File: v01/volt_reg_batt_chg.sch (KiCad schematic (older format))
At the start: 13 parts

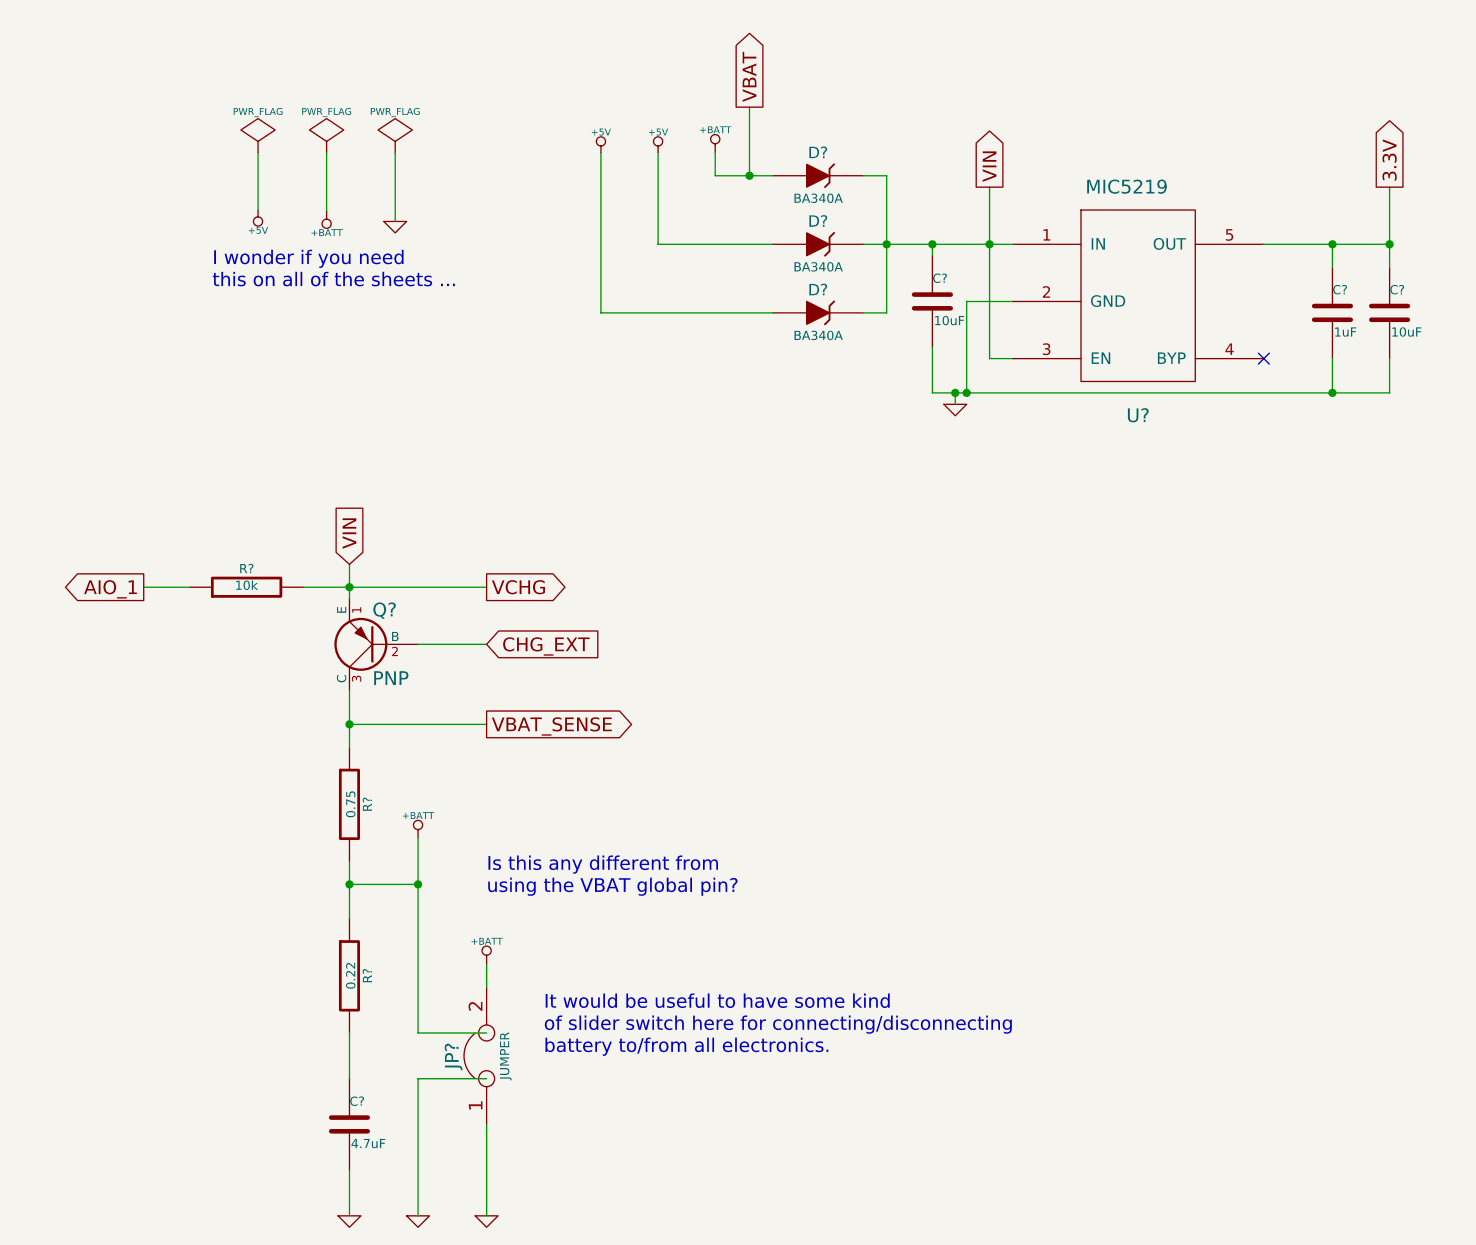
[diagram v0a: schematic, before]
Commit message: Basically just added a single DIP switch to battery charging circuit.
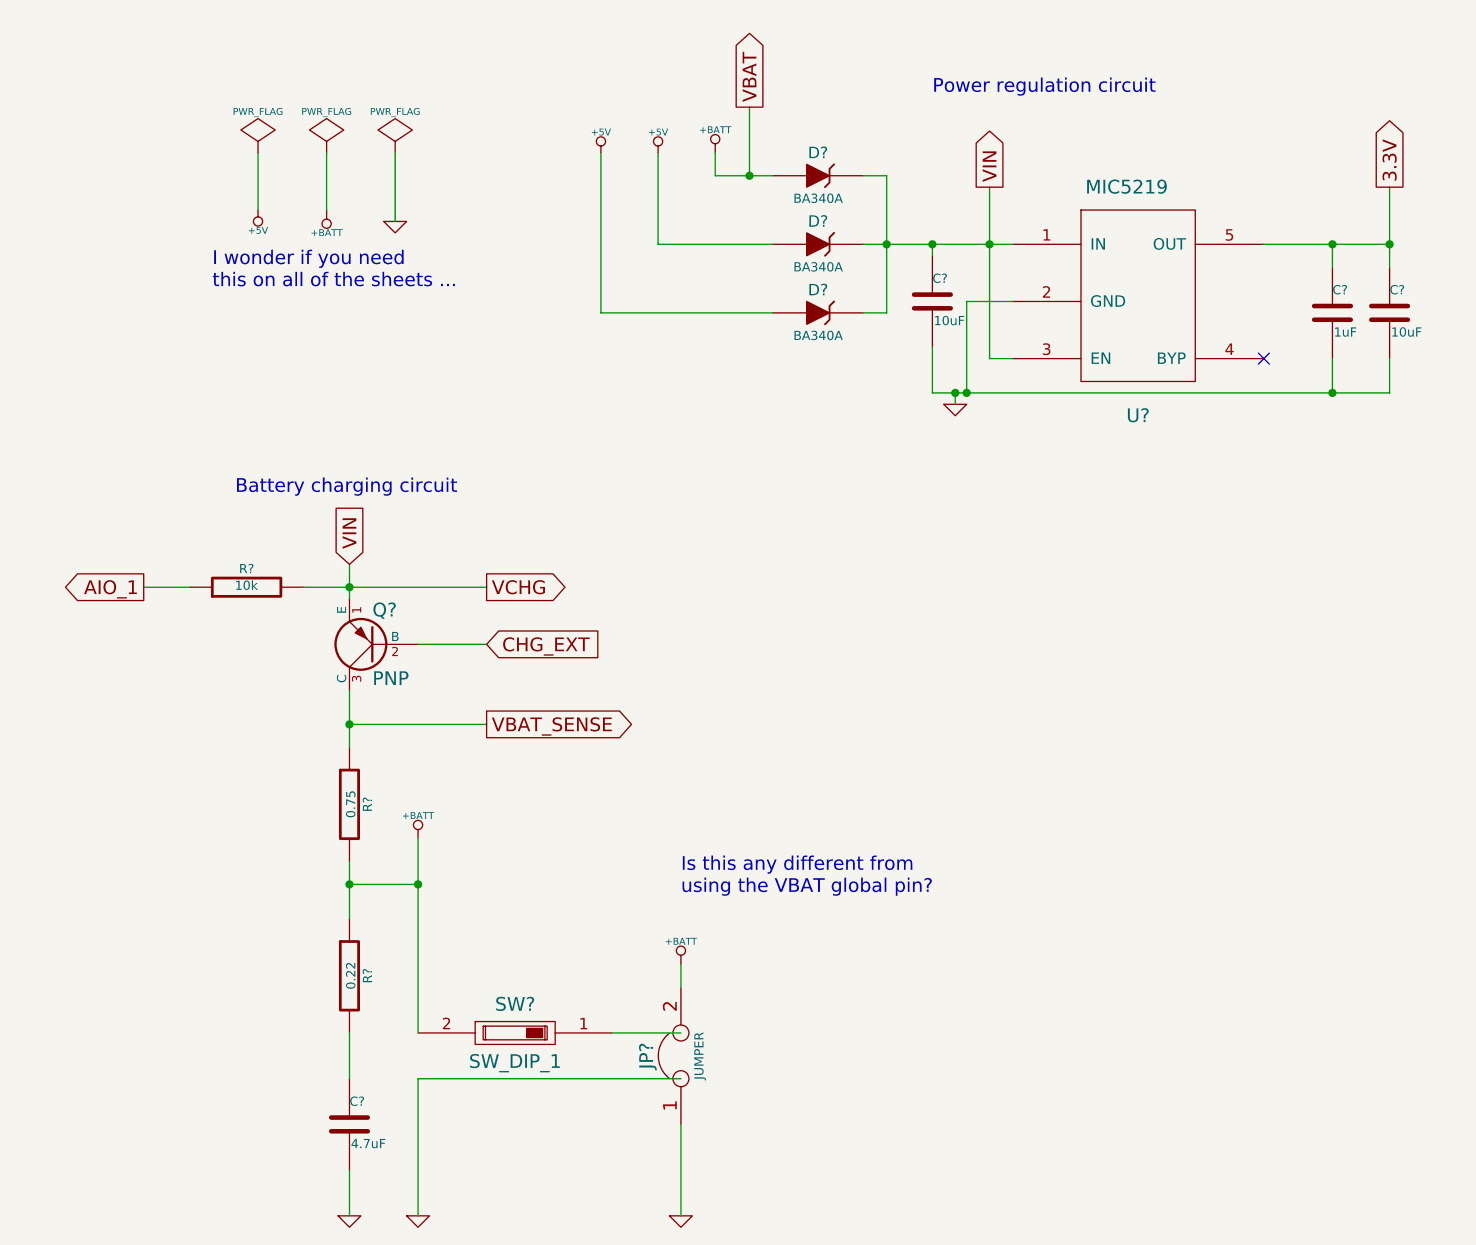
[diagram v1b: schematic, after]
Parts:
- added SW?: SW_DIP_1, symbol SW_DIP_1
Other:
- note added: "Battery charging circuit"
- note added: "Power regulation circuit"
- note removed: "It would be useful to have some kind \nof slider switch here for connecting/disconnecting \nbattery to/from all electronics."
- moved on the sheet: JP?
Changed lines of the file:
@@
 Sheet 4 4
 Title ""
-Date "12 oct 2014"
+Date "18 oct 2014"
 Rev ""
 Comp ""
@@
 L JUMPER JP?
 U 1 1 5439CFCC
-P 2850 5550
-F 0 "JP?" H 2850 5700 60  0000 C CNN
-F 1 "JUMPER" H 2850 5470 40  0000 C CNN
-F 2 "~" H 2850 5550 60  0000 C CNN
-F 3 "~" H 2850 5550 60  0000 C CNN
-	1    2850 5550
+P 3700 5550
+F 0 "JP?" H 3700 5700 60  0000 C CNN
+F 1 "JUMPER" H 3700 5470 40  0000 C CNN
+F 2 "~" H 3700 5550 60  0000 C CNN
+F 3 "~" H 3700 5550 60  0000 C CNN
+	1    3700 5550
 	0    -1   -1   0
 $EndComp
@@
 L GND #PWR?
 U 1 1 5439D2F7
-P 2850 6250
-F 0 "#PWR?" H 2850 6250 30  0001 C CNN
-F 1 "GND" H 2850 6180 30  0001 C CNN
-F 2 "" H 2850 6250 60  0000 C CNN
-F 3 "" H 2850 6250 60  0000 C CNN
-	1    2850 6250
+P 3700 6250
+F 0 "#PWR?" H 3700 6250 30  0001 C CNN
+F 1 "GND" H 3700 6180 30  0001 C CNN
+F 2 "" H 3700 6250 60  0000 C CNN
+F 3 "" H 3700 6250 60  0000 C CNN
+	1    3700 6250
 	1    0    0    -1
 $EndComp
@@
 L +BATT #PWR?
 U 1 1 5439D33F
-P 2850 5150
-F 0 "#PWR?" H 2850 5100 20  0001 C CNN
-F 1 "+BATT" H 2850 5250 30  0000 C CNN
-F 2 "" H 2850 5150 60  0000 C CNN
-F 3 "" H 2850 5150 60  0000 C CNN
-	1    2850 5150
+P 3700 5150
+F 0 "#PWR?" H 3700 5100 20  0001 C CNN
+F 1 "+BATT" H 3700 5250 30  0000 C CNN
+F 2 "" H 3700 5150 60  0000 C CNN
+F 3 "" H 3700 5150 60  0000 C CNN
+	1    3700 5150
 	1    0    0    -1
 $EndComp
@@
 Text GLabel 1350 3500 0    60   Output ~ 0
 AIO_1
+Text Notes 1650 2200 0    60   ~ 0
+I wonder if you need\nthis on all of the sheets ...
+Text Notes 3700 4850 0    60   ~ 0
+Is this any different from \nusing the VBAT global pin?
 Wire Wire Line
 	4500 2000 5150 2000
@@
 	2250 3950 2250 4200
 Wire Wire Line
-	4100 1700 3850 1700
+	3850 1700 4100 1700
 Wire Wire Line
 	3850 1700 3850 1600
@@
 	2250 3400 2250 3550
 Wire Wire Line
-	2550 5450 2850 5450
+	3400 5450 3700 5450
 Wire Wire Line
 	2550 4600 2550 5450
@@
 Connection ~ 2250 4800
 Wire Wire Line
-	2550 5650 2850 5650
-Wire Wire Line
 	2550 5650 2550 6250
 Connection ~ 2550 4800
@@
 Connection ~ 2250 3500
 Wire Wire Line
-	2850 5850 2850 6250
-Wire Wire Line
-	2850 5150 2850 5250
+	3700 5850 3700 6250
+Wire Wire Line
+	3700 5150 3700 5250
 Wire Wire Line
 	4000 1400 4000 1700
@@
 Wire Wire Line
 	1550 3500 1350 3500
-Text Notes 3100 5550 0    60   ~ 0
-It would be useful to have some kind \nof slider switch here for connecting/disconnecting \nbattery to/from all electronics.
-Text Notes 1650 2200 0    60   ~ 0
-I wonder if you need\nthis on all of the sheets ...
-Text Notes 2850 4850 0    60   ~ 0
-Is this any different from \nusing the VBAT global pin?
+$Comp
+L SW_DIP_1 SW?
+U 1 1 5442B59A
+P 2975 5450
+F 0 "SW?" H 2975 5575 60  0000 C CNN
+F 1 "SW_DIP_1" H 2975 5325 60  0000 C CNN
+F 2 "" H 2975 5450 60  0000 C CNN
+F 3 "" H 2975 5450 60  0000 C CNN
+	1    2975 5450
+	1    0    0    -1
+$EndComp
+Text Notes 1750 3100 0    60   ~ 0
+Battery charging circuit
+Text Notes 4800 1350 0    60   ~ 0
+Power regulation circuit
+Wire Wire Line
+	2550 5650 3700 5650
 $EndSCHEMATC

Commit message: ERC.
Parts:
- removed D?: BA340A, ~, symbol ZENER
- removed SW?: SW_DIP_1, symbol SW_DIP_1
- gave numbers to parts that had none: 12
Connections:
- net labels added: 5V_USB
- wire segments 43 -> 40
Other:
- note added: "I wonder if you need\nthis on all of the sheets ... No."
- note added: "It would be useful to have some kind \nof slider switch here for connecting/disconnecting \nbattery to/from all electronics."
- note added: "So, the voltages (+5V, GND, +BATT) are considered power inputs,\n while the power flags are considered power outputs. So, throughout\nthe schematic, components need to specify power pins as power input\n pins because they are being driven by the power flag (power output) \nnot the voltages (power input).\n"
- note removed: "Battery charging circuit"
- note removed: "I wonder if you need\nthis on all of the sheets ..."
- note removed: "Power regulation circuit"
- moved on the sheet: JP1

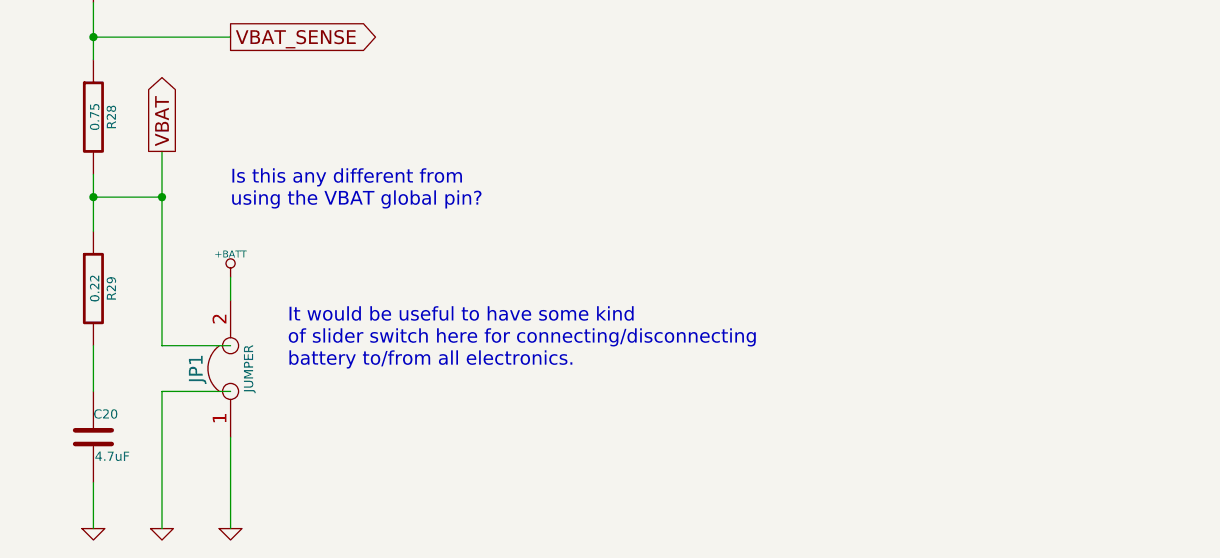
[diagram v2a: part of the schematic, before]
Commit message: updates:
1) added DIP-1 switch to connect/disconnect battery
2) annotated components in the entire schematic
3) generated netlist for the schematic
4) matched components with footprints (caps, DIP switch, diodes, LEDs, I think that's it ...)
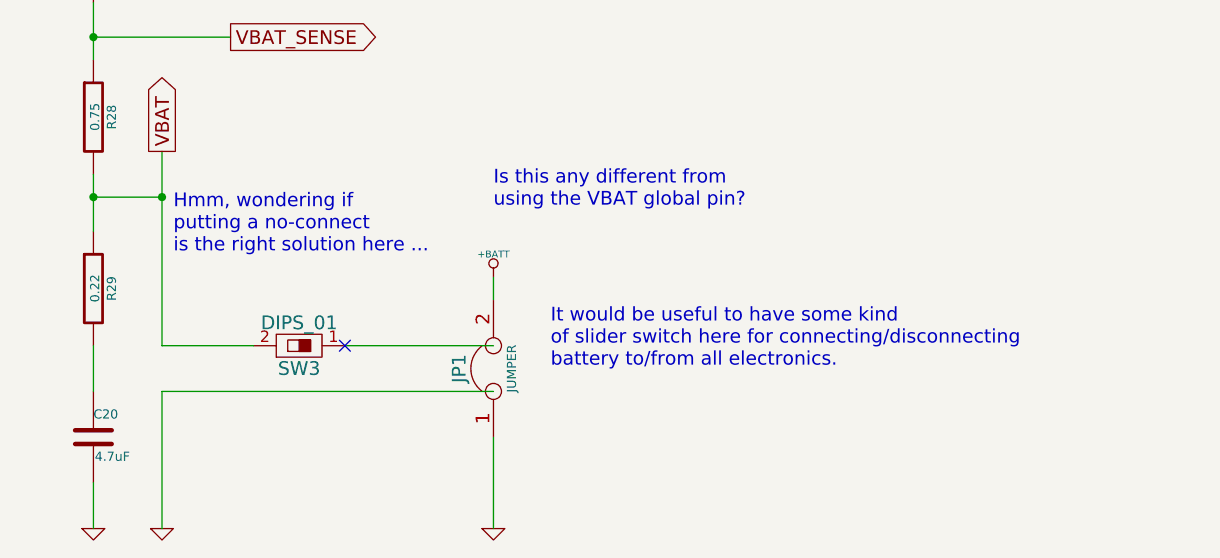
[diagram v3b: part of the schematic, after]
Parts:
- added SW3: DIPS_01, symbol DIPS_01
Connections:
- wire segments 40 -> 41
- no-connect marks 1 -> 2
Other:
- note added: "Hmm, wondering if \nputting a no-connect\nis the right solution here ..."
- moved on the sheet: JP1
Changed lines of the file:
@@
 LIBS:BC127
 LIBS:mic5219
+LIBS:ab2_usb
 LIBS:CWIEM_PCB_v01-cache
 EELAYER 27 0
@@
 L JUMPER JP1
 U 1 1 5439CFCC
-P 2850 5550
-F 0 "JP1" H 2850 5700 60  0000 C CNN
-F 1 "JUMPER" H 2850 5470 40  0000 C CNN
-F 2 "~" H 2850 5550 60  0000 C CNN
-F 3 "~" H 2850 5550 60  0000 C CNN
-	1    2850 5550
+P 4000 5550
+F 0 "JP1" H 4000 5700 60  0000 C CNN
+F 1 "JUMPER" H 4000 5470 40  0000 C CNN
+F 2 "~" H 4000 5550 60  0000 C CNN
+F 3 "~" H 4000 5550 60  0000 C CNN
+	1    4000 5550
 	0    -1   -1   0
 $EndComp
@@
 L GND #PWR018
 U 1 1 5439D2F7
-P 2850 6250
-F 0 "#PWR018" H 2850 6250 30  0001 C CNN
-F 1 "GND" H 2850 6180 30  0001 C CNN
-F 2 "" H 2850 6250 60  0000 C CNN
-F 3 "" H 2850 6250 60  0000 C CNN
-	1    2850 6250
+P 4000 6250
+F 0 "#PWR018" H 4000 6250 30  0001 C CNN
+F 1 "GND" H 4000 6180 30  0001 C CNN
+F 2 "" H 4000 6250 60  0000 C CNN
+F 3 "" H 4000 6250 60  0000 C CNN
+	1    4000 6250
 	1    0    0    -1
 $EndComp
@@
 L +BATT #PWR019
 U 1 1 5439D33F
-P 2850 5150
-F 0 "#PWR019" H 2850 5100 20  0001 C CNN
-F 1 "+BATT" H 2850 5250 30  0000 C CNN
-F 2 "" H 2850 5150 60  0000 C CNN
-F 3 "" H 2850 5150 60  0000 C CNN
-	1    2850 5150
+P 4000 5150
+F 0 "#PWR019" H 4000 5100 20  0001 C CNN
+F 1 "+BATT" H 4000 5250 30  0000 C CNN
+F 2 "" H 4000 5150 60  0000 C CNN
+F 3 "" H 4000 5150 60  0000 C CNN
+	1    4000 5150
 	1    0    0    -1
 $EndComp
@@
 	2250 3400 2250 3550
 Wire Wire Line
-	2550 5450 2850 5450
+	3350 5450 4000 5450
 Wire Wire Line
 	2550 4600 2550 5450
@@
 Connection ~ 2250 4800
 Wire Wire Line
-	2550 5650 2850 5650
+	2550 5650 4000 5650
 Wire Wire Line
 	2550 5650 2550 6250
@@
 Connection ~ 2250 3500
 Wire Wire Line
-	2850 5850 2850 6250
-Wire Wire Line
-	2850 5150 2850 5250
+	4000 5850 4000 6250
+Wire Wire Line
+	4000 5150 4000 5250
 Connection ~ 4000 1700
 Wire Wire Line
 	1550 3500 1350 3500
-Text Notes 3100 5550 0    60   ~ 0
+Text Notes 4250 5550 0    60   ~ 0
 It would be useful to have some kind \nof slider switch here for connecting/disconnecting \nbattery to/from all electronics.
 Text Notes 1300 2200 0    60   ~ 0
 I wonder if you need\nthis on all of the sheets ... No.
-Text Notes 2850 4850 0    60   ~ 0
+Text Notes 4000 4850 0    60   ~ 0
 Is this any different from \nusing the VBAT global pin?
 Wire Wire Line
@@
 Wire Wire Line
 	3550 2300 4100 2300
+Wire Wire Line
+	2550 5450 2950 5450
+$Comp
+L DIPS_01 SW3
+U 1 1 544BE30E
+P 3150 5450
+F 0 "SW3" V 3050 5450 60  0000 C CNN
+F 1 "DIPS_01" V 3250 5450 60  0000 C CNN
+F 2 "" H 3150 5450 60  0000 C CNN
+F 3 "" H 3150 5450 60  0000 C CNN
+	1    3150 5450
+	0    -1   -1   0
+$EndComp
+NoConn ~ 3350 5450
+Text Notes 2600 5050 0    60   ~ 0
+Hmm, wondering if \nputting a no-connect\nis the right solution here ...
 $EndSCHEMATC

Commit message: Updating with latest edits (haven't committed in a while)
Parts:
- removed JP1: JUMPER, ~, symbol JUMPER
- added P13: JST-PH2, jst-ph-JST-PH2, symbol JST-PH2
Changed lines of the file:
@@
 LIBS:mic5219
 LIBS:ab2_usb
+LIBS:jst-ph
 LIBS:CWIEM_PCB_v01-cache
 EELAYER 27 0
@@
 Sheet 4 4
 Title ""
-Date "25 oct 2014"
+Date "7 dec 2014"
 Rev ""
 Comp ""
@@
 $EndComp
 $Comp
-L GND #PWR013
+L GND #PWR18
 U 1 1 5439B1A3
 P 4900 2700
-F 0 "#PWR013" H 4900 2700 30  0001 C CNN
+F 0 "#PWR18" H 4900 2700 30  0001 C CNN
 F 1 "GND" H 4900 2630 30  0001 C CNN
 F 2 "" H 4900 2700 60  0000 C CNN
@@
 $EndComp
 $Comp
-L GND #PWR014
+L GND #PWR15
 U 1 1 5439B578
 P 2250 6250
-F 0 "#PWR014" H 2250 6250 30  0001 C CNN
+F 0 "#PWR15" H 2250 6250 30  0001 C CNN
 F 1 "GND" H 2250 6180 30  0001 C CNN
 F 2 "" H 2250 6250 60  0000 C CNN
@@
 3.3V
 $Comp
-L PWR_FLAG #FLG015
+L PWR_FLAG #FLG2
 U 1 1 5439CBDC
 P 2150 1600
-F 0 "#FLG015" H 2150 1695 30  0001 C CNN
+F 0 "#FLG2" H 2150 1695 30  0001 C CNN
 F 1 "PWR_FLAG" H 2150 1780 30  0000 C CNN
 F 2 "" H 2150 1600 60  0000 C CNN
@@
 $EndComp
 $Comp
-L +BATT #PWR016
+L +BATT #PWR14
 U 1 1 5439CC42
 P 2150 1850
-F 0 "#PWR016" H 2150 1800 20  0001 C CNN
+F 0 "#PWR14" H 2150 1800 20  0001 C CNN
 F 1 "+BATT" H 2150 1950 30  0000 C CNN
 F 2 "" H 2150 1850 60  0000 C CNN
@@
 VIN
 $Comp
-L JUMPER JP1
-U 1 1 5439CFCC
-P 4000 5550
-F 0 "JP1" H 4000 5700 60  0000 C CNN
-F 1 "JUMPER" H 4000 5470 40  0000 C CNN
-F 2 "~" H 4000 5550 60  0000 C CNN
-F 3 "~" H 4000 5550 60  0000 C CNN
-	1    4000 5550
-	0    -1   -1   0
-$EndComp
-$Comp
-L GND #PWR017
+L GND #PWR17
 U 1 1 5439D063
 P 2550 6250
-F 0 "#PWR017" H 2550 6250 30  0001 C CNN
+F 0 "#PWR17" H 2550 6250 30  0001 C CNN
 F 1 "GND" H 2550 6180 30  0001 C CNN
 F 2 "" H 2550 6250 60  0000 C CNN
@@
 Text GLabel 2850 3750 2    60   Input ~ 0
 CHG_EXT
-$Comp
-L GND #PWR018
-U 1 1 5439D2F7
-P 4000 6250
-F 0 "#PWR018" H 4000 6250 30  0001 C CNN
-F 1 "GND" H 4000 6180 30  0001 C CNN
-F 2 "" H 4000 6250 60  0000 C CNN
-F 3 "" H 4000 6250 60  0000 C CNN
-	1    4000 6250
-	1    0    0    -1
-$EndComp
-$Comp
-L +BATT #PWR019
-U 1 1 5439D33F
-P 4000 5150
-F 0 "#PWR019" H 4000 5100 20  0001 C CNN
-F 1 "+BATT" H 4000 5250 30  0000 C CNN
-F 2 "" H 4000 5150 60  0000 C CNN
-F 3 "" H 4000 5150 60  0000 C CNN
-	1    4000 5150
-	1    0    0    -1
-$EndComp
 $Comp
 L R R27
@@
 	2250 3400 2250 3550
 Wire Wire Line
-	3350 5450 4000 5450
+	3350 5450 3600 5450
 Wire Wire Line
 	2550 4600 2550 5450
@@
 Connection ~ 2250 4800
 Wire Wire Line
-	2550 5650 4000 5650
+	2550 5650 3600 5650
 Wire Wire Line
 	2550 5650 2550 6250
@@
 	2050 3500 2850 3500
 Connection ~ 2250 3500
-Wire Wire Line
-	4000 5850 4000 6250
-Wire Wire Line
-	4000 5150 4000 5250
 Connection ~ 4000 1700
 Wire Wire Line
 	1550 3500 1350 3500
-Text Notes 4250 5550 0    60   ~ 0
+Text Notes 4150 5500 0    60   ~ 0
 It would be useful to have some kind \nof slider switch here for connecting/disconnecting \nbattery to/from all electronics.
 Text Notes 1300 2200 0    60   ~ 0
@@
 	1850 1600 1850 1850
 $Comp
-L +5V #PWR020
+L +5V #PWR13
 U 1 1 5439CBF7
 P 1850 1850
-F 0 "#PWR020" H 1850 1940 20  0001 C CNN
+F 0 "#PWR13" H 1850 1940 20  0001 C CNN
 F 1 "+5V" H 1850 1940 30  0000 C CNN
 F 2 "" H 1850 1850 60  0000 C CNN
@@
 $EndComp
 $Comp
-L PWR_FLAG #FLG021
+L PWR_FLAG #FLG1
 U 1 1 5439CBEF
 P 1850 1600
-F 0 "#FLG021" H 1850 1695 30  0001 C CNN
+F 0 "#FLG1" H 1850 1695 30  0001 C CNN
 F 1 "PWR_FLAG" H 1850 1780 30  0000 C CNN
 F 2 "" H 1850 1600 60  0000 C CNN
@@
 	2450 1600 2450 1900
 $Comp
-L GND #PWR022
+L GND #PWR16
 U 1 1 5439CC8E
 P 2450 1900
-F 0 "#PWR022" H 2450 1900 30  0001 C CNN
+F 0 "#PWR16" H 2450 1900 30  0001 C CNN
 F 1 "GND" H 2450 1830 30  0001 C CNN
 F 2 "" H 2450 1900 60  0000 C CNN
@@
 $EndComp
 $Comp
-L PWR_FLAG #FLG023
+L PWR_FLAG #FLG3
 U 1 1 5439CBE9
 P 2450 1600
-F 0 "#FLG023" H 2450 1695 30  0001 C CNN
+F 0 "#FLG3" H 2450 1695 30  0001 C CNN
 F 1 "PWR_FLAG" H 2450 1780 30  0000 C CNN
 F 2 "" H 2450 1600 60  0000 C CNN
@@
 Text Notes 2600 5050 0    60   ~ 0
 Hmm, wondering if \nputting a no-connect\nis the right solution here ...
+$Comp
+L JST-PH2 P13
+U 1 1 5483E1A6
+P 3900 5600
+F 0 "P13" H 3800 5730 50  0000 L BNN
+F 1 "JST-PH2" H 3800 5310 50  0000 L BNN
+F 2 "jst-ph-JST-PH2" H 3900 5750 50  0001 C CNN
+F 3 "" H 3900 5600 60  0000 C CNN
+	1    3900 5600
+	-1   0    0    1
+$EndComp
+Wire Wire Line
+	3600 5650 3600 5600
+Wire Wire Line
+	3600 5450 3600 5500
 $EndSCHEMATC
